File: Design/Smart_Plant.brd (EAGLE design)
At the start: 66.3 x 128.6 mm, 22 parts, among them IC1 555

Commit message: Added design files for 'Kit' branch
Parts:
- removed C1: 10nF, rcl:C050-025X075
- removed C2: 470pF, rcl:C050-025X075
- removed C3: 1uF, rcl:E2,5-5
- removed D1: 1N4004, diode:DO41-10
- removed H1, H2: MOUNT-PAD-ROUND3.0, holes:3,0-PAD
- removed IC1: 555, SparkFun-IC-Special-Function:DIP08-KIT
- removed JMP1: 0R-JUMPB, jump-0r-smd:B0R-JMP
- removed LDR: VT20N1, photo-elements:TO46-VT200
- removed NTC: R1206, ptc-ntc:P640
- removed R1, R2, R6, R8: 10k, rcl:0207/10
- removed R3: 1k, rcl:0207/10
- removed R4: 330, rcl:0207/10
- removed R5: 1k6, rcl:0207/10
- removed R7: 1M, rcl:0207/10
- removed SJ1: (no value), jumper:SJ
- removed T1: (no value), transistor:TO92-ECB
- added J1: 455-1750-1-ND, SparkFun-Connectors:1X03
- added J2, J3: (no value), SparkFun-Connectors:1X04
- moved JP1 0.66 mm to (6.50, 34.0)
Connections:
- removed net EC_1: H1.B3,0, JP1.8
- removed net EC_2: H2.B3,0, JP1.9, R8.2
- removed net EXC: JMP1.1, JP1.12, R3.2
- removed net LIGHT: JP2.10, LDR.2, R1.2
- removed net MOIST: C3.+, D1.C, JP2.9, R7.1, SJ1.1
- removed net N$1: R3.1, T1.B
- removed net N$10: JMP1.3, T1.E
- removed net N$3: C2.1, IC1.2, IC1.6, R5.2
- removed net N$4: IC1.7, R4.2, R5.1
- removed net N$6: IC1.3, R6.1
- removed net N$9: C1.2, IC1.5
- removed net SIG: D1.A, R6.2, SJ1.2
- removed net TEMP: JP2.11, NTC.1, R2.2
- removed net VSENS: IC1.4, IC1.8, JMP1.2, LDR.1, NTC.2, R4.1
- new net A0: J1.3, JP1.1
- new net SCL: J2.2, J3.2, JP2.6
- new net SDA: J2.1, J3.1, JP2.3
- net 3V3: now also J1.2, J2.4, J3.4; no longer T1.C
- net GND: now also J1.1, J2.3, J3.3; no longer C1.1, C2.2, C3.-, IC1.1, R1.1, R2.1, R7.2, R8.1
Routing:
- net EC_1: track 145.5 -> 0.00 mm, vias 9 -> 0
- net EC_2: track 142.8 -> 0.00 mm, vias 9 -> 0
- net GND: track 110.3 -> 0.00 mm, vias 1 -> 0
- net A0: track 0.00 -> 78.9 mm, vias 0 -> 1
- net TEMP: track 74.8 -> 0.00 mm, vias 3 -> 0
- net SDA: track 0.00 -> 73.1 mm
- net SIG: track 68.4 -> 0.00 mm
- net SCL: track 0.00 -> 67.9 mm, vias 0 -> 2
- net LIGHT: track 66.7 -> 0.00 mm, vias 1 -> 0
- net 3V3: track 49.5 -> 100.2 mm, vias 1 -> 0
- net VSENS: track 50.4 -> 0.00 mm, vias 1 -> 0
- net EXC: track 37.1 -> 0.00 mm
- net N$6: track 31.2 -> 0.00 mm
- net N$3: track 29.2 -> 0.00 mm
- net MOIST: track 19.8 -> 0.00 mm
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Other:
- board size 66.3 x 128.6 mm -> 66.3 x 40.6 mm

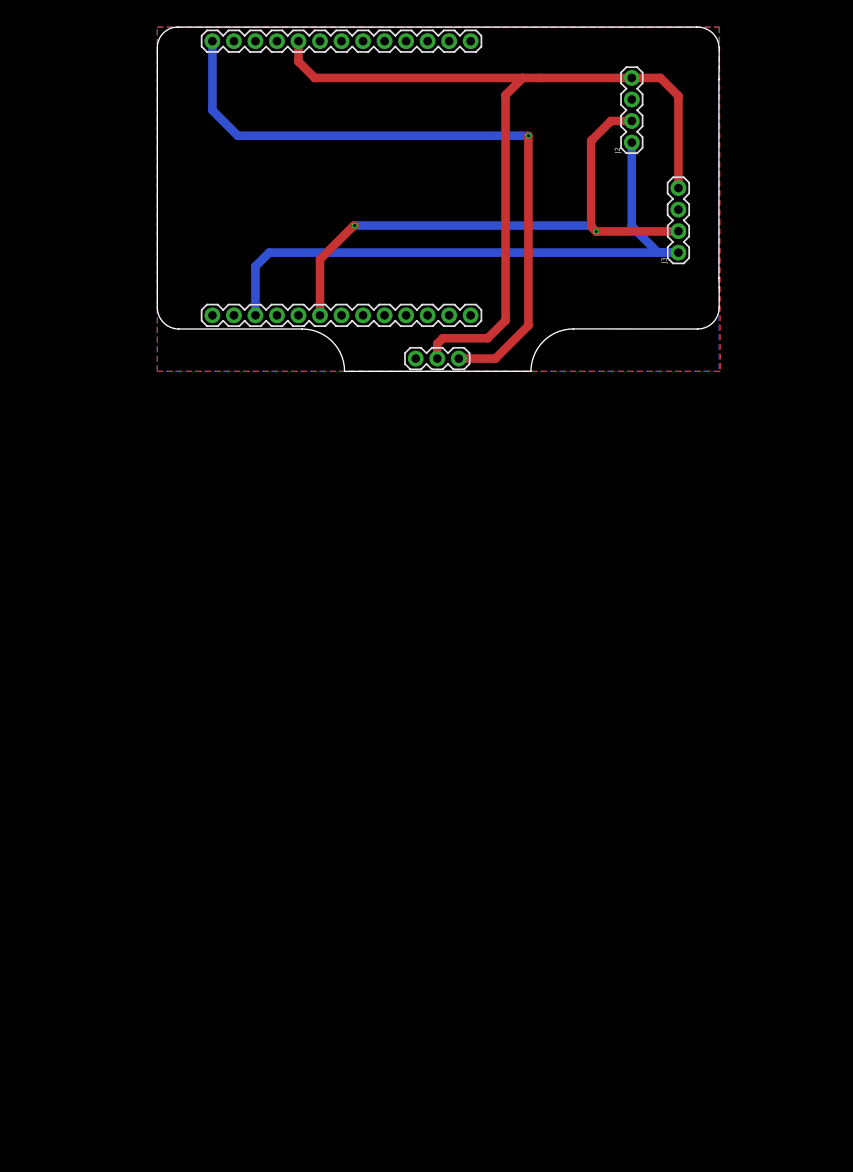
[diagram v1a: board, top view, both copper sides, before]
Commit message: Added design files to 'Custom' branch
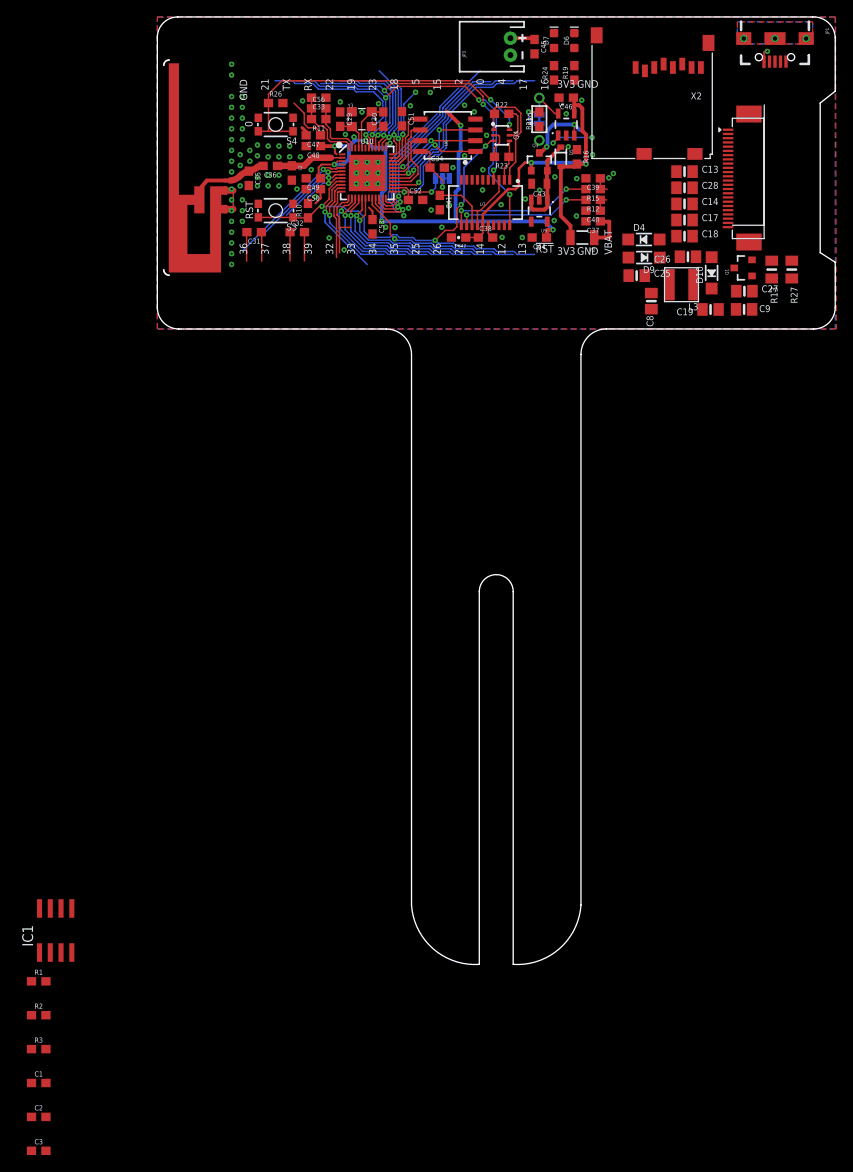
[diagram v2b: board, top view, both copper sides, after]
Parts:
- removed J1: 455-1750-1-ND, SparkFun-Connectors:1X03
- removed J2, J3: (no value), SparkFun-Connectors:1X04
- removed JP2: (no value), SparkFun-Connectors:1X13
- added C1, C2, C3, C34, C37, C38, C41, C48, C49, C51, C53: 0.1uF, SparkFun-Capacitors:0603
- added C13, C14, C17, C18, C19, C25, C27, C28, C9: 1uF, microbuilder:0805-NO
- added C26: 4.7uF/25V, microbuilder:0805-NO
- added C29, C30: 10pF, SparkFun-Capacitors:0603
- added C31, C32: 270pF, esp32-thing-temp:0603
- added C33: 10nF, SparkFun-Capacitors:0603
- added C35: 2.4pF, esp32-thing-temp:0603
- added C36: 5.6pF, esp32-thing-temp:0603
- added C39, C40: 47pF, SparkFun-Capacitors:0603
- added C42: 4.7uF, SparkFun-Capacitors:0603-CAP
- added C43: 1.0uF, SparkFun-Capacitors:0805
- added C44: 2.2uF, SparkFun-Capacitors:0603
- added C45, C46: 4.7uF, SparkFun-Capacitors:0603
- added C47: 100pF, SparkFun-Capacitors:0603
- added C50: 10uF, SparkFun-Capacitors:0603
- added C52: 1.0uF, SparkFun-Capacitors:0603
- added C56: 3.0nF, esp32-thing-temp:0603
- added C8: 10uF/10V+, microbuilder:0805-NO
- added D10, D4, D9: MBR0530, microbuilder:SOD-123
- added D5: BAT20J, SparkFun-DiscreteSemi:SOD-323
- added D6: Yellow, SparkFun-LED:LED-0603
- added D7: Green, SparkFun-LED:LED-0603
- added E2: ANTENNA, esp32-thing-temp:TRACE_ANTENNA_2.4GHZ_25.7MM_TUNED
- added EINK1: EINK_24PIN_290IN, microbuilder:EINK_290IN
- added F2: 500mA, SparkFun-PowerIC:PTC-1206
- added IC1: NE555D, linear:SO08
- added JP3: LiPo, SparkFun-Connectors:JST-2-PTH
- added L2: 2.7nH, SparkFun-Passives:0603
- added L3: 10uH, microbuilder:INDUCTOR_4X4MM_NR401
- added Q1: IRLML0100, Parts:SOT23-3
- added Q3: 2.5A/30V, SparkFun-DiscreteSemi:SOT23-3
- added Q4: MBT3904DW1T1, esp32-thing-temp:SC70-6
- added R1, R12, R15, R2, R3: 27, SparkFun-Resistors:0603
- added R10, R16, R22, R23, R26: 10k, SparkFun-Resistors:0603
- added R11: 20k, SparkFun-Resistors:0603
- added R13: 0.47ohm, microbuilder:0805_10MGAP
- added R19, R24: 1K, SparkFun-Resistors:0603
- added R20: 2.0k, SparkFun-Resistors:0603
- added R21: DNP, SparkFun-Passives:1/6W-RES
- added R27: DNP, microbuilder:0805_10MGAP
- added S3: RESET, SparkFun-Electromechanical:TACTILE_SWITCH_SMD_4.6X2.8MM
- added S4: BTN-0, SparkFun-Electromechanical:TACTILE_SWITCH_SMD_4.6X2.8MM
- added SJ4: (no value), SparkFun-Passives:PAD-JUMPER-3-2OF3_NC_BY_TRACE_YES_SILK_FULL_BOX
- added SJ5: JUMPER-PAD-2-NC_BY_TRACE, SparkFun-Passives:PAD-JUMPER-2-NC_BY_TRACE_YES_SILK
- added U10: ESP3212, esp32-thing-temp:QFN48-0.4MM
- added U6: W25Q32FVSS, SparkFun-DigitalIC:SOIC-8
- added U7: FT231XS, SparkFun-DigitalIC:SSOP20_L
- added U8: MCP73831, SparkFun-PowerIC:SOT23-5
- added U9: AP2112K-3.3V, SparkFun-PowerIC:SOT23-5
- added X2: MICROSD, microbuilder:MICROSD
- added Y3: 26MHz, things:CRYSTAL-SMD-3.2X2.5
- JP1: device SparkFun-Connectors:1X13 -> SparkFun-Connectors:USB-B-MICRO-SMD_V03
- moved JP1 66.4 mm to (72.9, 34.3), turned to 270 degrees
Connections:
- removed net A0: J1.3, JP1.1
- removed net SCL: J2.2, J3.2, JP2.6
- removed net SDA: J2.1, J3.1, JP2.3
- new net 0: Q4.6, R26.1, S4.3, S4.4, U10.23
- new net 12: U10.18
- new net 19: U10.38
- new net 21: U10.42
- new net 22: U10.39
- new net 25: U10.14
- new net 26: U10.15
- new net 27: U10.16
- new net 3.3V_F: C41.1, U7.13, U7.14, U7.3
- new net 32: U10.12
- new net 33: U10.13
- new net 34: U10.10
- new net 35: U10.11
- new net 36: C31.2, U10.5
- new net 37: C31.1, U10.6
- new net 38: C32.1, U10.7
- new net 39: C32.2, U10.8
- new net BUSY: EINK1.9, U10.24
- new net CAP_10N1: C33.2, C56.1, R11.2, U10.48
- new net CHIP_PU: Q4.3, R10.1, S3.3, S3.4, U10.9
- new net D+: C39.1, JP1.D+, R15.1
- new net D-: C40.1, JP1.D-, R12.1
- new net DC: EINK1.11, U10.27
- new net DISPCS: EINK1.12, U10.34
- new net DTR: Q4.1, R22.1, U7.1
- new net FLASH_SCK: U10.31, U6.6
- new net FLASH_SCS: U10.30, U6.1
- new net FLASH_SDI: U10.33, U6.5
- new net FLASH_SDO: U10.32, U6.2
- new net FLASH_SHD: U10.28, U6.7
- new net FLASH_SWP: U10.29, U6.3
- new net FLASH_VDD: C52.1, SJ4.1, U10.26
- new net GDR: EINK1.2, Q1.1
- new net LNA_IN1: C36.1, L2.1, U10.2
- new net MISO_SD: U10.22, X2.7
- new net MOSI: EINK1.14, U10.36
- new net MOSI_SD: U10.21, X2.3
- new net N$11: C9.2, EINK1.5
- new net N$12: C13.2, EINK1.18
- new net N$13: C14.2, EINK1.20
- new net N$14: C17.2, EINK1.22
- new net N$15: C18.2, EINK1.24
- new net N$16: C26.2, D4.A, D9.C
- new net N$17: C26.1, D10.A, L3.P$1, Q1.3
- new net N$18: R15.2, U7.11
- new net N$19: D6.A, R19.2
- new net N$20: D6.C, U8.1
- new net N$21: R21.2, SJ5.2, U8.5
- new net N$22: R20.2, SJ5.1
- new net N$23: Q4.5, R22.2
- new net N$24: Q4.2, R23.2
- new net N$25: C29.2, U10.45, Y3.1
- new net N$26: C30.2, U10.44, Y3.3
- new net N$27: D7.A, R24.2
- new net N$30: C56.2, R11.1, U10.47
- new net N$31: C27.2, EINK1.4
- new net N$32: C28.2, EINK1.19
- new net N$5: C34.1, SJ4.2, U6.8
- new net N$6: R12.2, U7.12
- new net RESE: EINK1.3, Q1.2, R13.1, R27.1
- new net RESET: EINK1.10, U10.25
- new net RTS: Q4.4, R23.1, U7.2
- new net SCLK: EINK1.13, U10.35
- new net SCLK_SD: U10.17, X2.5
- new net SDCS_SD: U10.20, X2.2
- new net SHIELD: JP1.SHIELD1, JP1.SHIELD2, JP1.SHIELD3
- new net TRACE_ANT1: C35.1, C36.2, E2.ANT
- new net TSCL: EINK1.6
- new net TSDA: EINK1.7
- new net U0RXD: U10.40, U7.20
- new net U0TXD: U10.41, U7.4
- new net V+: IC1.8
- new net VGH: C19.1, D10.C, EINK1.21
- new net VGL: C25.1, D9.A, EINK1.23
- new net VIN: C43.1, D5.C, Q3.2, U9.1, U9.3
- new net VUSB-RAW: C37.1, F2.1, JP1.VBUS
- new net V_BATT: C45.1, JP3.2, Q3.3, U8.3
- new net V_USB: C38.1, C42.1, C46.1, D5.A, F2.2, Q3.1, R16.2, R19.1, U7.15, U8.4
- net 3V3: now also C44.1, C47.1, C48.1, C49.1, C50.1, C51.1, C53.1, C8.2, EINK1.15, EINK1.16, L3.P$2, R10.2, R24.1, R26.2, SJ4.3, U10.1, U10.19, U10.3, U10.37, U10.4, U10.43, U10.46, U9.5, X2.4; no longer J1.2, J2.4, J3.4, JP1.5
- net GND: now also C13.1, C14.1, C17.1, C18.1, C19.2, C25.2, C27.1, C28.1, C29.1, C30.1, C33.1, C34.2, C35.2, C37.2, C38.2, C39.2, C40.2, C41.2, C42.2, C43.2, C44.2, C45.2, C46.2, C47.2, C48.2, C49.2, C50.2, C51.2, C52.2, C53.2, C8.1, C9.1, D4.C, D7.C, E2.GND, E2.GND2, EINK1.17, EINK1.8, IC1.1, JP1.GND, JP3.1, L2.2, R13.2, R16.1, R20.1, R21.1, R27.2, S3.1, S3.2, S4.1, S4.2, U10.EP, U6.4, U7.16, U7.6, U8.2, U9.2, X2.6, X2.MT1, X2.MT2, Y3.2, Y3.4; no longer J1.1, J2.3, J3.3, JP1.13
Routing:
- net A0: track 78.9 -> 0.00 mm, vias 1 -> 0
- net SDA: track 73.1 -> 0.00 mm
- net SCL: track 67.9 -> 0.00 mm, vias 2 -> 0
- net 0: track 0.00 -> 62.2 mm, vias 0 -> 3
- net CHIP_PU: track 0.00 -> 56.5 mm, vias 0 -> 4
- net U0RXD: track 0.00 -> 45.4 mm, vias 0 -> 4
- net V_USB: track 0.00 -> 43.1 mm, vias 0 -> 2
- net U0TXD: track 0.00 -> 41.0 mm, vias 0 -> 4
- net 3V3: track 100.2 -> 74.1 mm, vias 0 -> 8
- net RESET: track 0.00 -> 25.7 mm, vias 0 -> 1
- net DC: track 0.00 -> 22.6 mm, vias 0 -> 1
- net BUSY: track 0.00 -> 21.5 mm, vias 0 -> 1
- net 12: track 0.00 -> 20.9 mm, vias 0 -> 1
- net MISO_SD: track 0.00 -> 20.8 mm, vias 0 -> 1
- net SDCS_SD: track 0.00 -> 20.7 mm, vias 0 -> 1
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- added copper zone on layer 1, net SHIELD
- added copper zone on layer 16, net SHIELD
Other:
- board size 66.3 x 40.6 mm -> 80 x 111.8 mm
- board text added: "!RST!"
- board text added: "0"
- board text added: "12"
- board text added: "13"
- board text added: "14"
- board text added: "15"
- board text added: "16"
- board text added: "17"
- board text added: "18"
- board text added: "19"
- board text added: "2"
- board text added: "21"
- board text added: "22"
- board text added: "23"
- board text added: "25"
- board text added: "26"
- board text added: "27"
- board text added: "32"
- board text added: "33"
- board text added: "34"
- board text added: "35"
- board text added: "36"
- board text added: "37"
- board text added: "38"
- board text added: "39"
- board text added: "3V3"
- board text added: "4"
- board text added: "5"
- board text added: "Adafruit Industries"
- board text added: "CHG PROG"
- board text added: "E-Ink Display"
- board text added: "FLASH VCC"
- board text added: "GND"
- board text added: "IC"
- board text added: "RST"
- board text added: "RX"
- board text added: "RXI"
- board text added: "TX"
- board text added: "TXO"
- board text added: "VBAT"
- board text added: "VUSB"
